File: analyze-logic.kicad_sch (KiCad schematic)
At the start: 27 parts, among them J1 Input 0 - 7, J2 Input 8 - 15, J3 Connector Oscilloscope, U1 MC33375ST-3.3T3G

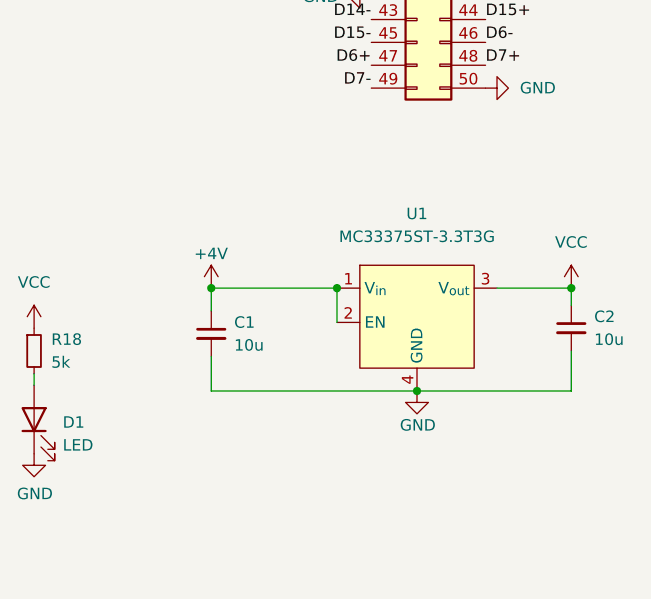
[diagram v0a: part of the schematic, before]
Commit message: added board and begin with traces
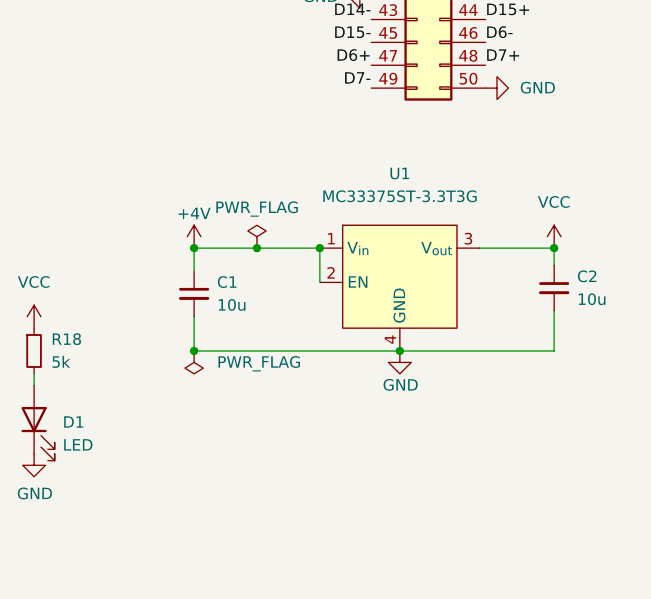
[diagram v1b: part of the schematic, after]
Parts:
- C1, C2: footprint (none) -> Capacitor_SMD:C_0603_1608Metric
- D1: footprint (none) -> Diode_SMD:D_0603_1608Metric
- J1, J2: footprint (none) -> Connector_IDC:IDC-Header_2x08_P2.54mm_Vertical; MOUSER_NR (none) -> DNO
- J3: footprint (none) -> Connector_IDC:IDC-Header_2x25_P2.54mm_Vertical; MOUSER_NR (none) -> DNO
- R1, R10, R11, R12, R13, R14, R15, R16, R17, R18, R2, R3, R4, R5, R6, R7, R8, R9: footprint (none) -> Resistor_SMD:R_0402_1005Metric
- RN1, RN2: footprint (none) -> Resistor_SMD:R_Array_Convex_8x0602
- U1: footprint (none) -> Package_TO_SOT_SMD:SOT-223
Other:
- moved on the sheet: C1, C2, U1

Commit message: added mouser nr to schematic
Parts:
- C1, C2: MOUSER_NR (none) -> 81-GRM188D71A106KA3D
- R1, R10, R11, R12, R13, R14, R15, R16, R17, R2, R3, R4, R5, R6, R7, R8, R9: MOUSER_NR (none) -> 667-ERJ-2GEJ101X
- R18: MOUSER_NR (none) -> 71-RCC04024K70FKED
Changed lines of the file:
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@@
+      (effects (font (size 1.27 1.27)) hide)
+    )
+    (property "MOUSER_NR" "667-ERJ-2GEJ101X" (id 4) (at 152.4 35.56 0)
       (effects (font (size 1.27 1.27)) hide)
     )
@@
       (effects (font (size 1.27 1.27)) hide)
     )
+    (property "MOUSER_NR" "71-RCC04024K70FKED" (id 4) (at 207.645 139.7 0)
+      (effects (font (size 1.27 1.27)) hide)
+    )
     (pin "1")
     (pin "2")
@@
       (effects (font (size 1.27 1.27)) hide)
     )
+    (property "MOUSER_NR" "667-ERJ-2GEJ101X" (id 4) (at 195.58 25.4 0)
+      (effects (font (size 1.27 1.27)) hide)
+    )
     (pin "1")
     (pin "2")
@@
       (effects (font (size 1.27 1.27)) hide)
     )
+    (property "MOUSER_NR" "667-ERJ-2GEJ101X" (id 4) (at 132.08 46.99 0)
+      (effects (font (size 1.27 1.27)) hide)
+    )
     (pin "1")
     (pin "2")
@@
     )
     (property "Datasheet" "~" (id 3) (at 195.58 35.56 0)
+      (effects (font (size 1.27 1.27)) hide)
+    )
+    (property "MOUSER_NR" "667-ERJ-2GEJ101X" (id 4) (at 195.58 35.56 0)
       (effects (font (size 1.27 1.27)) hide)
     )
@@
       (effects (font (size 1.27 1.27)) hide)
     )
+    (property "MOUSER_NR" "667-ERJ-2GEJ101X" (id 4) (at 195.58 46.99 0)
+      (effects (font (size 1.27 1.27)) hide)
+    )
     (pin "1")
     (pin "2")
@@
     )
     (property "Datasheet" "~" (id 3) (at 173.99 35.56 0)
+      (effects (font (size 1.27 1.27)) hide)
+    )
+    (property "MOUSER_NR" "667-ERJ-2GEJ101X" (id 4) (at 173.99 35.56 0)
       (effects (font (size 1.27 1.27)) hide)
     )
@@
       (effects (font (size 1.27 1.27)) hide)
     )
+    (property "MOUSER_NR" "667-ERJ-2GEJ101X" (id 4) (at 173.99 58.42 0)
+      (effects (font (size 1.27 1.27)) hide)
+    )
     (pin "1")
     (pin "2")
@@
       (effects (font (size 1.27 1.27)) hide)
     )
+    (property "MOUSER_NR" "667-ERJ-2GEJ101X" (id 4) (at 152.4 58.42 0)
+      (effects (font (size 1.27 1.27)) hide)
+    )
     (pin "1")
     (pin "2")
@@
     )
     (property "Datasheet" "~" (id 3) (at 265.43 132.715 0)
+      (effects (font (size 1.27 1.27)) hide)
+    )
+    (property "MOUSER_NR" "81-GRM188D71A106KA3D" (id 4) (at 265.43 132.715 0)
       (effects (font (size 1.27 1.27)) hide)
     )
@@
       (effects (font (size 1.27 1.27)) hide)
     )
+    (property "MOUSER_NR" "667-ERJ-2GEJ101X" (id 4) (at 195.58 68.58 0)
+      (effects (font (size 1.27 1.27)) hide)
+    )
     (pin "1")
     (pin "2")
@@
     )
     (property "Datasheet" "~" (id 3) (at 173.99 25.4 0)
+      (effects (font (size 1.27 1.27)) hide)
+    )
+    (property "MOUSER_NR" "667-ERJ-2GEJ101X" (id 4) (at 173.99 25.4 0)
       (effects (font (size 1.27 1.27)) hide)
     )
@@
       (effects (font (size 1.27 1.27)) hide)
     )
+    (property "MOUSER_NR" "667-ERJ-2GEJ101X" (id 4) (at 132.08 25.4 0)
+      (effects (font (size 1.27 1.27)) hide)
+    )
     (pin "1")
     (pin "2")
@@
       (effects (font (size 1.27 1.27)) hide)
     )
+    (property "MOUSER_NR" "667-ERJ-2GEJ101X" (id 4) (at 132.08 35.56 0)
+      (effects (font (size 1.27 1.27)) hide)
+    )
     (pin "1")
     (pin "2")
@@
       (effects (font (size 1.27 1.27)) hide)
     )
+    (property "MOUSER_NR" "667-ERJ-2GEJ101X" (id 4) (at 173.99 46.99 0)
+      (effects (font (size 1.27 1.27)) hide)
+    )
     (pin "1")
     (pin "2")
@@
       (effects (font (size 1.27 1.27)) hide)
     )
+    (property "MOUSER_NR" "667-ERJ-2GEJ101X" (id 4) (at 195.58 58.42 0)
+      (effects (font (size 1.27 1.27)) hide)
+    )
     (pin "1")
     (pin "2")
@@
       (effects (font (size 1.27 1.27)) hide)
     )
+    (property "MOUSER_NR" "667-ERJ-2GEJ101X" (id 4) (at 152.4 25.4 0)
+      (effects (font (size 1.27 1.27)) hide)
+    )
     (pin "1")
     (pin "2")
@@
       (effects (font (size 1.27 1.27)) hide)
     )
+    (property "MOUSER_NR" "667-ERJ-2GEJ101X" (id 4) (at 152.4 46.99 0)
+      (effects (font (size 1.27 1.27)) hide)
+    )
     (pin "1")
     (pin "2")
@@
     )
     (property "Datasheet" "~" (id 3) (at 132.08 58.42 0)
+      (effects (font (size 1.27 1.27)) hide)
+    )
+    (property "MOUSER_NR" "667-ERJ-2GEJ101X" (id 4) (at 132.08 58.42 0)
       (effects (font (size 1.27 1.27)) hide)
     )
@@
       (effects (font (size 1.27 1.27)) hide)
     )
+    (property "MOUSER_NR" "81-GRM188D71A106KA3D" (id 4) (at 225.425 133.35 0)
+      (effects (font (size 1.27 1.27)) hide)
+    )
